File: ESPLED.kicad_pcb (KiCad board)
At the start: 2 copper layers, 115.5 x 59 mm, 32 parts, among them J1 PWM-1, J2 PWM-2, J3 PWM-3, J4 PWM-4, J5 GND, J6 12V, J7 5V-Stb, Q1 AO D403, Q2 BSS138, Q3 BSS138, Q4 AO D403, Q5 AO D403, Q6 AO D403, U1 mini_esp32, X1 234-503, X2 234-503

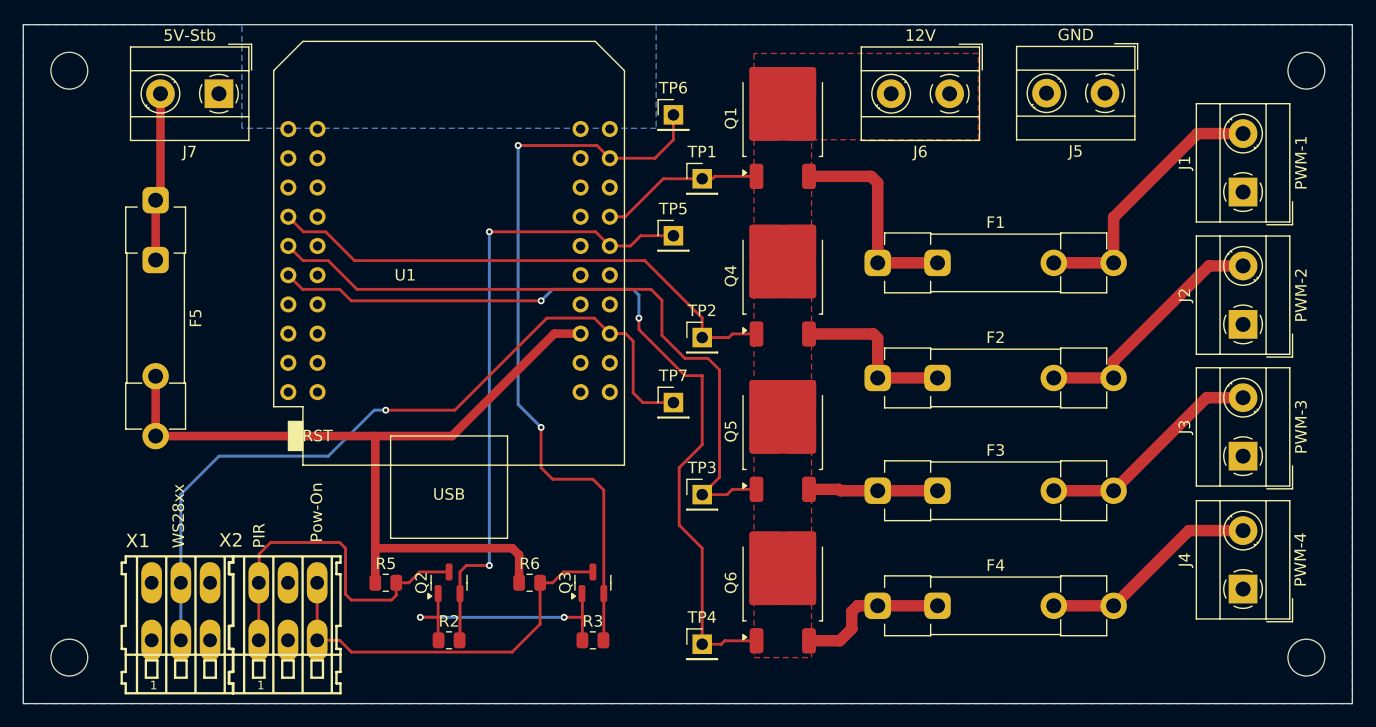
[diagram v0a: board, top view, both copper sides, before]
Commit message: Changed PIR from IO12 (strapping pin) to IO13
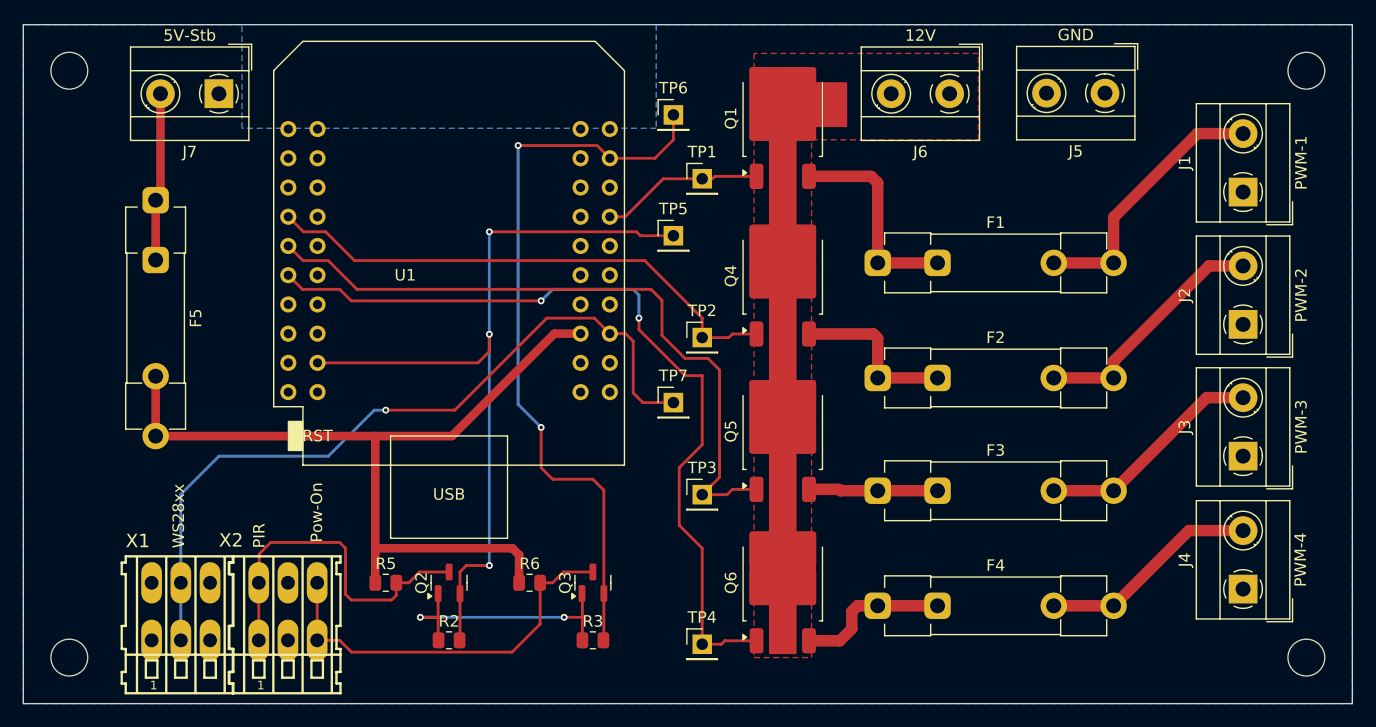
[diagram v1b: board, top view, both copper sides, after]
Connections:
- U1 pad 18: unconnected-(U1-IO_13/TCK-Pad18) -> MCU_PIR
- U1 pad 30: MCU_PIR -> unconnected-(U1-IO_12/TDI-Pad30)
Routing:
- net MCU_PIR: track 54.6 -> 70.7 mm, vias 2 -> 3
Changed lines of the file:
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@@
 	(net 48 "unconnected-(U1-IO_36{slash}SVP{slash}A0-Pad4)")
 	(net 49 "unconnected-(U1-IO_05{slash}D8-Pad14)")
-	(net 50 "unconnected-(U1-IO_13{slash}TCK-Pad18)")
+	(net 50 "unconnected-(U1-IO_12{slash}TDI-Pad30)")
 	(net 51 "unconnected-(U1-IO_19{slash}D6-Pad10)")
 	(footprint "Package_TO_SOT_SMD:SOT-23"
@@
 			(layers "*.Cu" "*.Mask")
 			(remove_unused_layers no)
-			(net 50 "unconnected-(U1-IO_13{slash}TCK-Pad18)")
+			(net 14 "MCU_PIR")
 			(pinfunction "IO_13/TCK")
 			(pintype "bidirectional")
@@
 			(layers "*.Cu" "*.Mask")
 			(remove_unused_layers no)
-			(net 14 "MCU_PIR")
+			(net 50 "unconnected-(U1-IO_12{slash}TDI-Pad30)")
 			(pinfunction "IO_12/TDI")
 			(pintype "bidirectional")
@@
 		)
 	)
+	(gr_rect
+		(start 141.9 37.1)
+		(end 145 40.8)
+		(stroke
+			(width 0.2)
+			(type solid)
+		)
+		(fill solid)
+		(layer "F.Cu")
+		(net 12)
+	)
+	(gr_rect
+		(start 138.4 38.1)
+		(end 140.6 86.6)
+		(stroke
+			(width 0.2)
+			(type solid)
+		)
+		(fill solid)
+		(layer "F.Cu")
+		(net 12)
+	)
 	(gr_line
 		(start 73.5 32)
@@
 	)
 	(segment
-		(start 127.16 50.34)
-		(end 126.27 51.23)
+		(start 113.01 61.39)
+		(end 99.07 61.39)
 		(width 0.25)
 		(layer "F.Cu")
@@
 	)
 	(segment
-		(start 114 79)
-		(end 112 79)
+		(start 127.14 50.34)
+		(end 126.8 50)
 		(width 0.25)
 		(layer "F.Cu")
@@
 	)
 	(segment
-		(start 126.27 51.23)
-		(end 124.47 51.23)
+		(start 129.9975 50.34)
+		(end 127.14 50.34)
 		(width 0.25)
 		(layer "F.Cu")
@@
 	)
 	(segment
-		(start 111.45 79.55)
-		(end 111.45 81.4375)
+		(start 114 79)
+		(end 112 79)
 		(width 0.25)
 		(layer "F.Cu")
@@
 	)
 	(segment
-		(start 129.9975 50.34)
-		(end 127.16 50.34)
+		(start 111.45 79.55)
+		(end 111.45 81.4375)
 		(width 0.25)
 		(layer "F.Cu")
@@
 	)
 	(segment
-		(start 123.24 50)
-		(end 124.47 51.23)
+		(start 114 60.4)
+		(end 113.01 61.39)
 		(width 0.25)
 		(layer "F.Cu")
@@
 	)
 	(segment
-		(start 112 79)
-		(end 111.45 79.55)
+		(start 114 58.9)
+		(end 114 60.4)
 		(width 0.25)
 		(layer "F.Cu")
@@
 	)
 	(segment
-		(start 114 50)
-		(end 123.24 50)
+		(start 126.8 50)
+		(end 114 50)
+		(width 0.25)
+		(layer "F.Cu")
+		(net 14)
+	)
+	(segment
+		(start 112 79)
+		(end 111.45 79.55)
 		(width 0.25)
 		(layer "F.Cu")
@@
 		(net 14)
 	)
+	(via
+		(at 114 58.9)
+		(size 0.6)
+		(drill 0.3)
+		(layers "F.Cu" "B.Cu")
+		(net 14)
+	)
 	(segment
 		(start 114 50)
+		(end 114 58.9)
+		(width 0.25)
+		(layer "B.Cu")
+		(net 14)
+	)
+	(segment
+		(start 114 58.9)
 		(end 114 79)
 		(width 0.25)
